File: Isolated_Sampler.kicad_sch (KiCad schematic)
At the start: 22 parts, among them U11 AMC1351, U13 TLV6002

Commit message: schematic: Assign all footprints
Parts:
- C42, C43: footprint (none) -> Capacitor_SMD:C_0603_1608Metric
- R74: footprint (none) -> Resistor_SMD:R_0603_1608Metric
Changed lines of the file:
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@@
 			)
 		)
-		(property "Footprint" ""
+		(property "Footprint" "Capacitor_SMD:C_0603_1608Metric"
 			(at 194.31 80.01 0)
 			(effects
@@
 			)
 		)
-		(property "Footprint" ""
+		(property "Footprint" "Resistor_SMD:R_0603_1608Metric"
 			(at 185.42 114.3 0)
 			(effects
@@
 			)
 		)
-		(property "Footprint" ""
+		(property "Footprint" "Capacitor_SMD:C_0603_1608Metric"
 			(at 180.34 114.3 0)
 			(effects

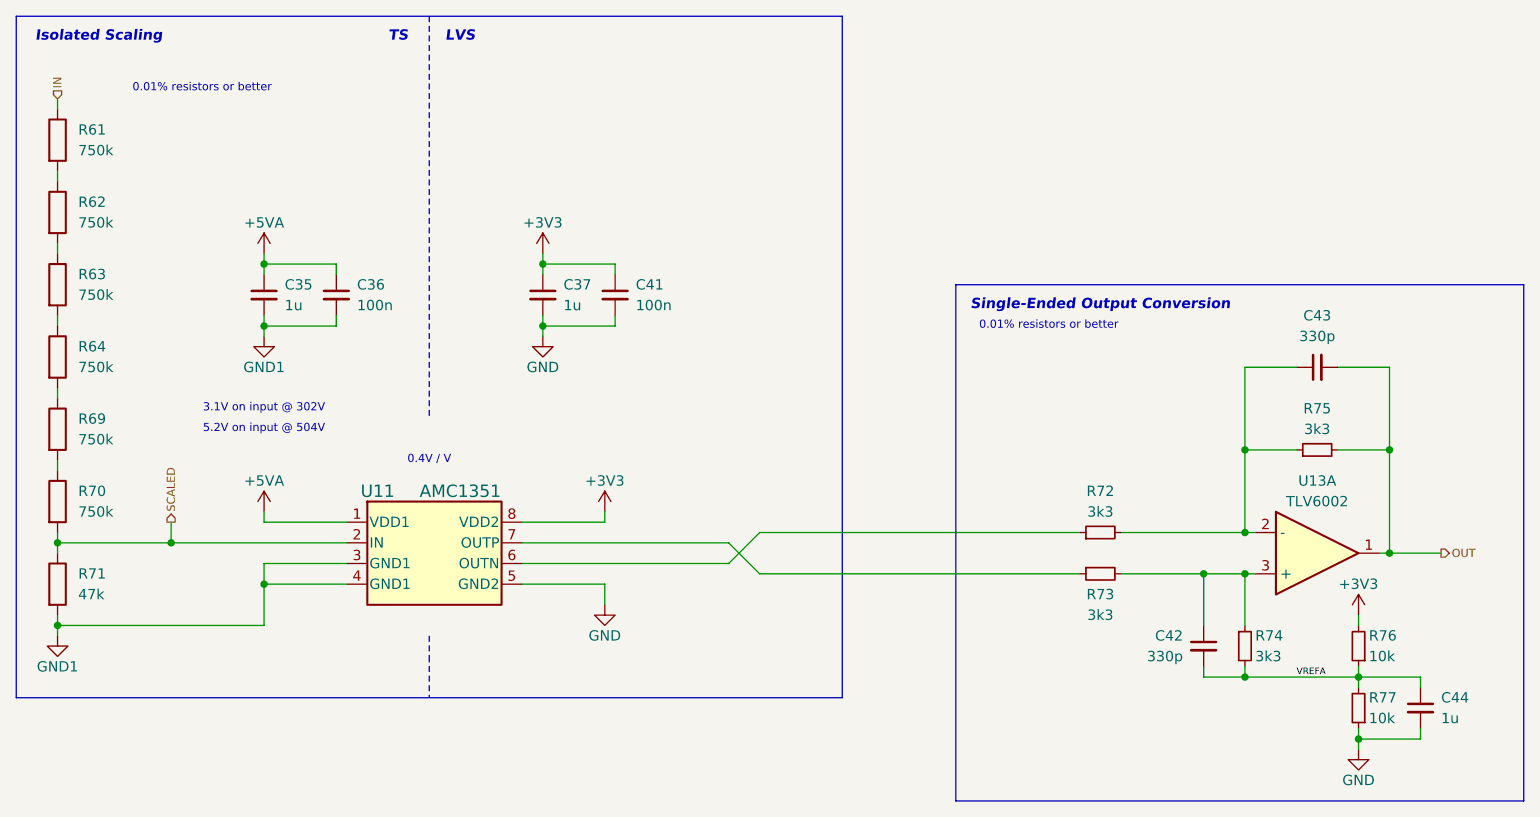
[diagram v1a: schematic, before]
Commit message: schematic: Reassign reference designators
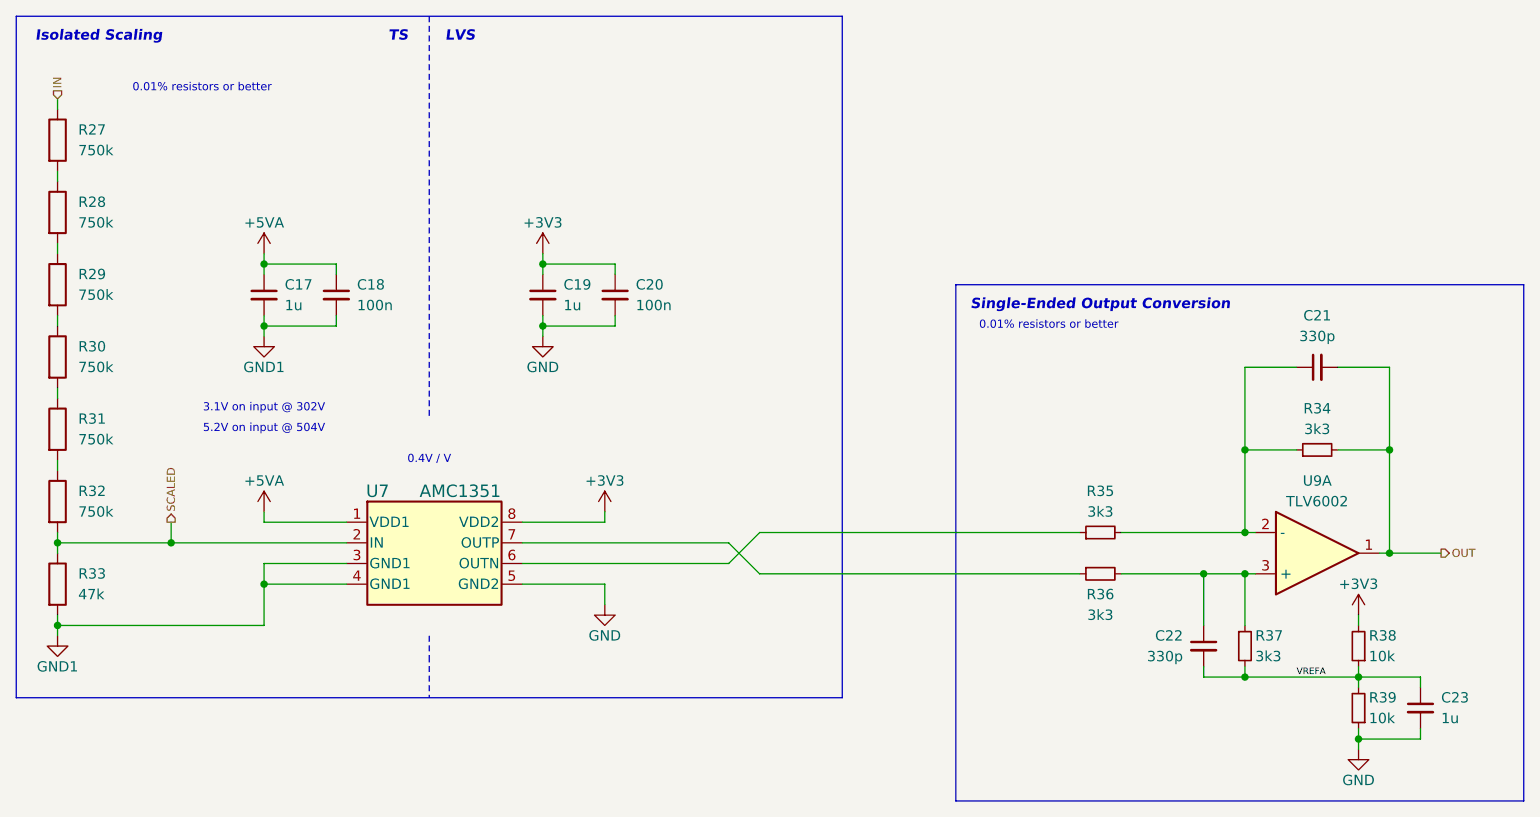
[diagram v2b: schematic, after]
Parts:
- renumbered C35 to C17, C36 to C18, C37 to C19, C41 to C20, C43 to C21, C42 to C22, C44 to C23, R61 to R27, R62 to R28, R63 to R29, R64 to R30, R69 to R31, R70 to R32, R71 to R33, R75 to R34, R72 to R35, R73 to R36, R74 to R37, R76 to R38, R77 to R39, U11 to U7, U13 to U9

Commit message: schematic: Fill out most of the BOM
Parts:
- C18, C20: Dist # C5199872 -> C1591; Mfr # CL10B105KB8NQNC -> CL10B104KB8NNNC
- C23: Dist (none) -> LCSC; Dist # (none) -> C5199872; Mfr (none) -> Samsung; Mfr # (none) -> CL10B105KB8NQNC
- R38, R39: Dist (none) -> LCSC; Dist # (none) -> C25804; Mfr (none) -> Uni-Royal; Mfr # (none) -> 0603WAF1002T5E
- U7: Dist (none) -> Mouser; Dist # (none) -> 595-AMC1351QDWVRQ1; Mfr (none) -> Texas Instruments; Mfr # (none) -> AMC1351QDWVRQ1
- U9: Dist (none) -> Mouser; Dist # (none) -> 595-TLV6002QDRQ1; Mfr (none) -> Texas Instruments; Mfr # (none) -> TLV6002QDRQ1
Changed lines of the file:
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@@
 			)
 		)
-		(property "Dist #" "C5199872"
+		(property "Dist #" "C1591"
 			(at 107.95 71.12 0)
 			(effects
@@
 			)
 		)
-		(property "Mfr #" "CL10B105KB8NQNC"
+		(property "Mfr #" "CL10B104KB8NNNC"
 			(at 107.95 71.12 0)
 			(effects
@@
 			)
 		)
-		(property "Dist #" "C5199872"
+		(property "Dist #" "C1591"
 			(at 73.66 71.12 0)
 			(effects
@@
 			)
 		)
-		(property "Mfr #" "CL10B105KB8NQNC"
+		(property "Mfr #" "CL10B104KB8NNNC"
 			(at 73.66 71.12 0)
 			(effects
@@
 			)
 		)
+		(property "Dist" "Mouser"
+			(at 194.31 102.87 0)
+			(effects
+				(font
+					(size 1.27 1.27)
+				)
+				(hide yes)
+			)
+		)
+		(property "Dist #" "595-TLV6002QDRQ1"
+			(at 194.31 102.87 0)
+			(effects
+				(font
+					(size 1.27 1.27)
+				)
+				(hide yes)
+			)
+		)
+		(property "Mfr" "Texas Instruments"
+			(at 194.31 102.87 0)
+			(effects
+				(font
+					(size 1.27 1.27)
+				)
+				(hide yes)
+			)
+		)
+		(property "Mfr #" "TLV6002QDRQ1"
+			(at 194.31 102.87 0)
+			(effects
+				(font
+					(size 1.27 1.27)
+				)
+				(hide yes)
+			)
+		)
 		(pin "4"
 		)
@@
 			)
 		)
+		(property "Dist" "LCSC"
+			(at 207.01 121.92 0)
+			(effects
+				(font
+					(size 1.27 1.27)
+				)
+				(hide yes)
+			)
+		)
+		(property "Dist #" "C5199872"
+			(at 207.01 121.92 0)
+			(effects
+				(font
+					(size 1.27 1.27)
+				)
+				(hide yes)
+			)
+		)
+		(property "Mfr" "Samsung"
+			(at 207.01 121.92 0)
+			(effects
+				(font
+					(size 1.27 1.27)
+				)
+				(hide yes)
+			)
+		)
+		(property "Mfr #" "CL10B105KB8NQNC"
+			(at 207.01 121.92 0)
+			(effects
+				(font
+					(size 1.27 1.27)
+				)
+				(hide yes)
+			)
+		)
 		(pin "2"
 		)
@@
 			)
 		)
+		(property "Dist" "LCSC"
+			(at 199.39 114.3 0)
+			(effects
+				(font
+					(size 1.27 1.27)
+				)
+				(hide yes)
+			)
+		)
+		(property "Dist #" "C25804"
+			(at 199.39 114.3 0)
+			(effects
+				(font
+					(size 1.27 1.27)
+				)
+				(hide yes)
+			)
+		)
+		(property "Mfr" "Uni-Royal"
+			(at 199.39 114.3 0)
+			(effects
+				(font
+					(size 1.27 1.27)
+				)
+				(hide yes)
+			)
+		)
+		(property "Mfr #" "0603WAF1002T5E"
+			(at 199.39 114.3 0)
+			(effects
+				(font
+					(size 1.27 1.27)
+				)
+				(hide yes)
+			)
+		)
 		(pin "1"
 		)
@@
 		(property "Description" "Precision, 5-V Input, Reinforced Isolated Amplifier"
 			(at 77.216 77.978 0)
+			(effects
+				(font
+					(size 1.27 1.27)
+				)
+				(hide yes)
+			)
+		)
+		(property "Dist" "Mouser"
+			(at 77.47 96.52 0)
+			(effects
+				(font
+					(size 1.27 1.27)
+				)
+				(hide yes)
+			)
+		)
+		(property "Dist #" "595-AMC1351QDWVRQ1"
+			(at 77.47 96.52 0)
+			(effects
+				(font
+					(size 1.27 1.27)
+				)
+				(hide yes)
+			)
+		)
+		(property "Mfr" "Texas Instruments"
+			(at 77.47 96.52 0)
+			(effects
+				(font
+					(size 1.27 1.27)
+				)
+				(hide yes)
+			)
+		)
+		(property "Mfr #" "AMC1351QDWVRQ1"
+			(at 77.47 96.52 0)
 			(effects
 				(font
@@
 			(at 199.39 121.92 0)
 			(effects
+				(font
+					(size 1.27 1.27)
+				)
+				(hide yes)
+			)
+		)
+		(property "Dist" "LCSC"
+			(at 199.39 121.92 0)
+			(effects
+				(font
+					(size 1.27 1.27)
+				)
+				(hide yes)
+			)
+		)
+		(property "Dist #" "C25804"
+			(at 199.39 121.92 0)
+			(effects
+				(font
+					(size 1.27 1.27)
+				)
+				(hide yes)
+			)
+		)
+		(property "Mfr" "Uni-Royal"
+			(at 199.39 121.92 0)
+			(effects
+				(font
+					(size 1.27 1.27)
+				)
+				(hide yes)
+			)
+		)
+		(property "Mfr #" "0603WAF1002T5E"
+			(at 199.39 121.92 0)
+			(effects

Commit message: pcb: Setup net classes and import components
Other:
- company: (none) -> York Formula Student
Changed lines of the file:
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@@
 	(paper "A4")
 	(title_block
+		(date "2025-12-13")
 		(rev "${REVISION}")
+		(company "York Formula Student")
+		(comment 1 "Designed by Josh B, Logan C, and Owen S")
 	)
 	(rectangle

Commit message: Revision A
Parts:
- R27, R28, R29, R30, R31, R32, R33: footprint Resistor_SMD:R_0805_2012Metric -> Resistor_SMD:R_1206_3216Metric
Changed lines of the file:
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@@
 			)
 		)
-		(property "Footprint" "Resistor_SMD:R_0805_2012Metric"
+		(property "Footprint" "Resistor_SMD:R_1206_3216Metric"
 			(at 37.592 78.74 90)
 			(effects
@@
 			)
 		)
-		(property "Footprint" "Resistor_SMD:R_0805_2012Metric"
+		(property "Footprint" "Resistor_SMD:R_1206_3216Metric"
 			(at 37.592 60.96 90)
 			(effects
@@
 			)
 		)
-		(property "Footprint" "Resistor_SMD:R_0805_2012Metric"
+		(property "Footprint" "Resistor_SMD:R_1206_3216Metric"
 			(at 37.592 87.63 90)
 			(effects
@@
 			)
 		)
-		(property "Footprint" "Resistor_SMD:R_0805_2012Metric"
+		(property "Footprint" "Resistor_SMD:R_1206_3216Metric"
 			(at 37.592 96.52 90)
 			(effects
@@
 			)
 		)
-		(property "Footprint" "Resistor_SMD:R_0805_2012Metric"
+		(property "Footprint" "Resistor_SMD:R_1206_3216Metric"
 			(at 37.592 106.68 90)
 			(effects
@@
 			)
 		)
-		(property "Footprint" "Resistor_SMD:R_0805_2012Metric"
+		(property "Footprint" "Resistor_SMD:R_1206_3216Metric"
 			(at 37.592 69.85 90)
 			(effects
@@
 			)
 		)
-		(property "Footprint" "Resistor_SMD:R_0805_2012Metric"
+		(property "Footprint" "Resistor_SMD:R_1206_3216Metric"
 			(at 37.592 52.07 90)
 			(effects

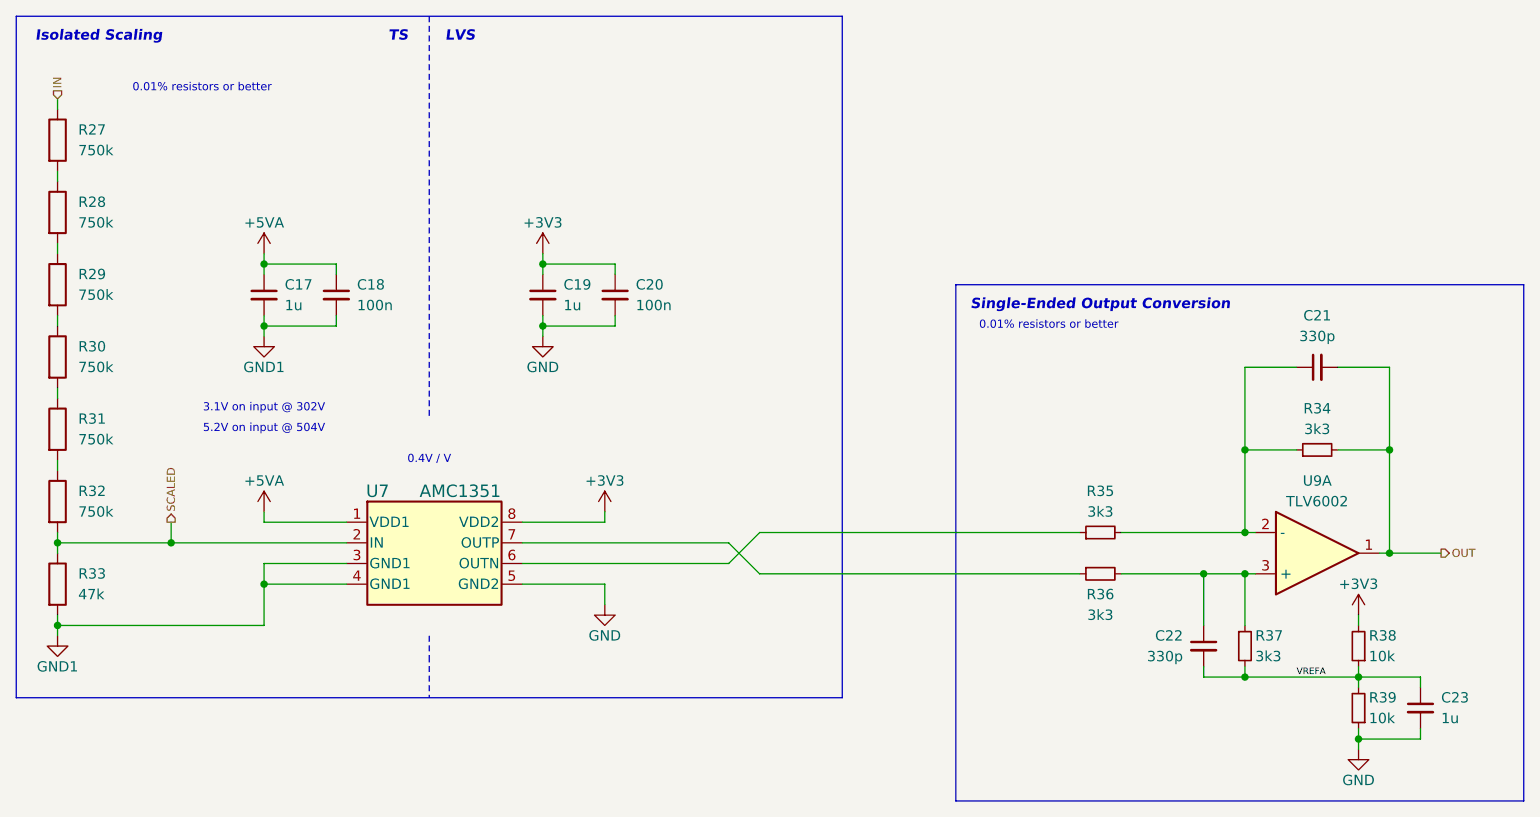
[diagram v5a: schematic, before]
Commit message: *: Add test points around sampling
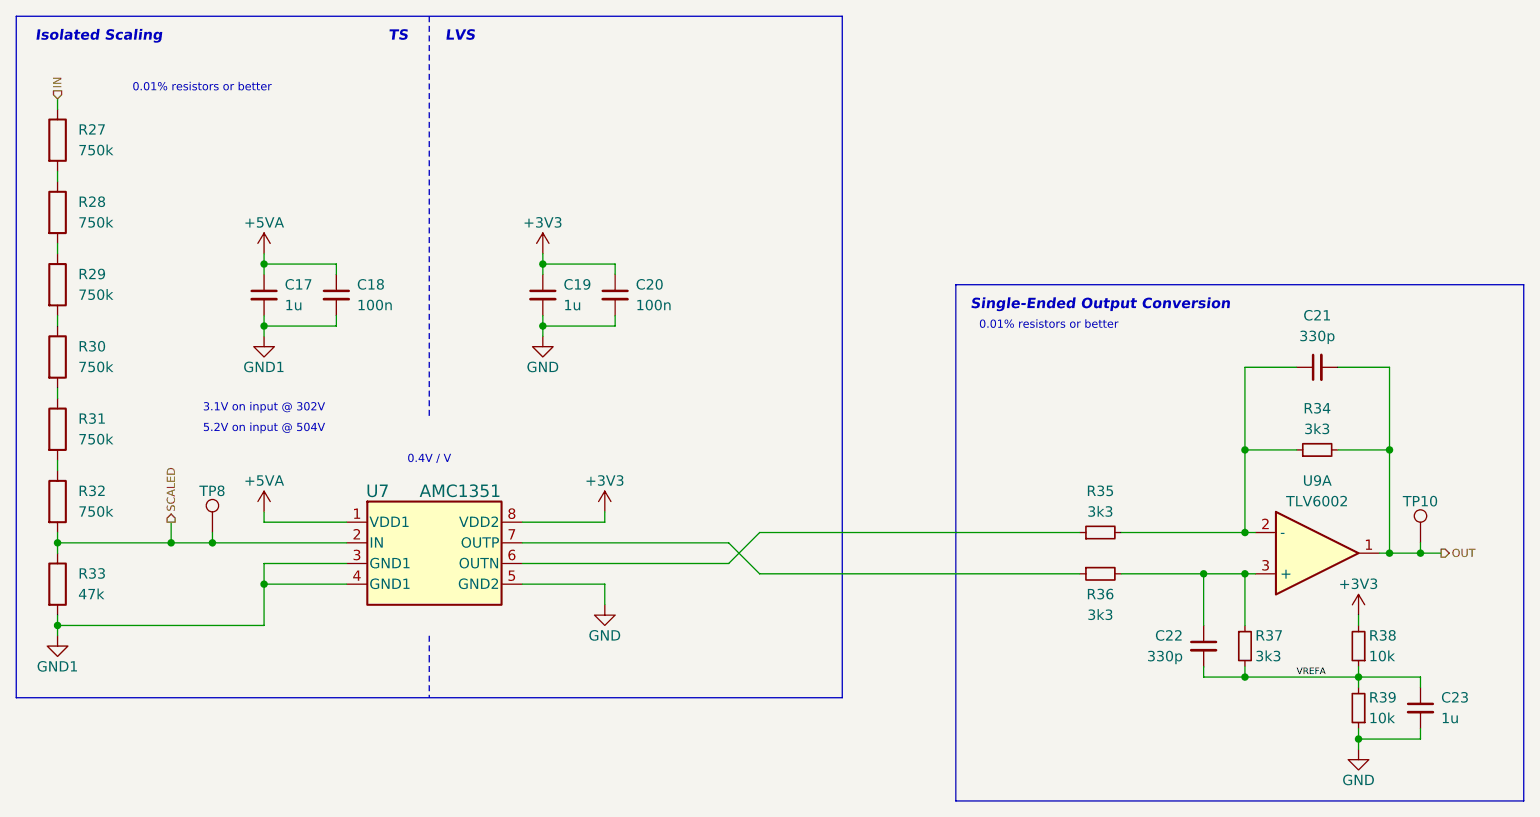
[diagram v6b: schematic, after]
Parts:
- added TP10, TP8: TestPoint, TestPoint:TestPoint_Keystone_5000-5004_Miniature, symbol Connector:TestPoint
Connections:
- net OUT: now also TP10.1
- net SCALED: now also TP8.1
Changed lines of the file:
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@@
+	)
+	(junction
+		(at 58.42 101.6)
+		(diameter 0)
+		(color 0 0 0 0)
 	)
 	(junction
@@
 	)
 	(junction
+		(at 207.01 102.87)
+		(diameter 0)
+		(color 0 0 0 0)
+	)
+	(junction
 		(at 180.34 105.41)
 		(diameter 0)
@@
 	(wire
 		(pts
+			(xy 58.42 100.33) (xy 58.42 101.6)
+		)
+		(stroke
+			(width 0)
+			(type default)
+		)
+	)
+	(wire
+		(pts
 			(xy 191.77 80.01) (xy 185.42 80.01)
 		)
@@
 	(wire
 		(pts
-			(xy 53.34 101.6) (xy 74.93 101.6)
+			(xy 53.34 101.6) (xy 58.42 101.6)
 		)
 		(stroke
@@
 	(wire
 		(pts
+			(xy 58.42 101.6) (xy 74.93 101.6)
+		)
+		(stroke
+			(width 0)
+			(type default)
+		)
+	)
+	(wire
+		(pts
 			(xy 203.2 80.01) (xy 203.2 90.17)
 		)
@@
 	(wire
 		(pts
-			(xy 203.2 102.87) (xy 209.55 102.87)
+			(xy 207.01 102.87) (xy 209.55 102.87)
+		)
+		(stroke
+			(width 0)
+			(type default)
+		)
+	)
+	(wire
+		(pts
+			(xy 203.2 102.87) (xy 207.01 102.87)
 		)
 		(stroke
@@
 		(pts
 			(xy 64.77 66.04) (xy 64.77 67.31)
+		)
+		(stroke
+			(width 0)
+			(type default)
+		)
+	)
+	(wire
+		(pts
+			(xy 207.01 101.6) (xy 207.01 102.87)
 		)
 		(stroke
@@
 	)
 	(symbol
+		(lib_id "Connector:TestPoint")
+		(at 207.01 101.6 0)
+		(unit 1)
+		(exclude_from_sim no)
+		(in_bom yes)
+		(on_board yes)
+		(dnp no)
+		(property "Reference" "TP10"
+			(at 207.01 96.52 0)
+			(effects
+				(font
+					(size 1.27 1.27)
+				)
+			)
+		)
+		(property "Value" "TestPoint"
+			(at 209.55 99.5679 0)
+			(effects
+				(font
+					(size 1.27 1.27)
+				)
+				(justify left)
+				(hide yes)
+			)
+		)
+		(property "Footprint" "TestPoint:TestPoint_Keystone_5000-5004_Miniature"
+			(at 212.09 101.6 0)
+			(effects
+				(font
+					(size 1.27 1.27)
+				)
+				(hide yes)
+			)
+		)
+		(property "Datasheet" "~"
+			(at 212.09 101.6 0)
+			(effects
+				(font
+					(size 1.27 1.27)
+				)
+				(hide yes)
+			)
+		)
+		(property "Description" "test point"
+			(at 207.01 101.6 0)
+			(effects
+				(font
+					(size 1.27 1.27)
+				)
+				(hide yes)
+			)
+		)
+		(pin "1"
+		)
+		(instances
+			(project "Precharge_PCB"
+				(path "/c467677d-b98c-4488-bd11-965ef67263b2/5111e28e-8231-41c0-b506-a567affaf28a/40675a50-a5c6-4759-acd6-914b3ce60c39"
+					(reference "TP10")
+					(unit 1)
+				)
+				(path "/c467677d-b98c-4488-bd11-965ef67263b2/5111e28e-8231-41c0-b506-a567affaf28a/481c6b85-c613-4759-b3cf-851f0c736d9a"
+					(reference "TP11")
+					(unit 1)
+				)
+			)
+		)
+	)
+	(symbol
 		(lib_id "Device:R_Small")
 		(at 167.64 100.33 90)
@@
 					(unit 1)
 				)
+			)
+		)
+	)
+	(symbol
+		(lib_id "Connector:TestPoint")
+		(at 58.42 100.33 0)
+		(unit 1)
+		(exclude_from_sim no)
+		(in_bom yes)
+		(on_board yes)
+		(dnp no)
+		(property "Reference" "TP8"
+			(at 58.42 95.25 0)
+			(effects
+				(font
+					(size 1.27 1.27)
+				)
+			)
+		)
+		(property "Value" "TestPoint"
+			(at 60.96 98.2979 0)
+			(effects
+				(font
+					(size 1.27 1.27)
+				)
+				(justify left)
+				(hide yes)
+			)
+		)
+		(property "Footprint" "TestPoint:TestPoint_Keystone_5000-5004_Miniature"
+			(at 63.5 100.33 0)
+			(effects
+				(font
+					(size 1.27 1.27)
+				)
+				(hide yes)
+			)
+		)
+		(property "Datasheet" "~"
+			(at 63.5 100.33 0)
+			(effects
+				(font
+					(size 1.27 1.27)
+				)
+				(hide yes)
+			)
+		)
+		(property "Description" "test point"
+			(at 58.42 100.33 0)
+			(effects
+				(font
+					(size 1.27 1.27)
+				)
+				(hide yes)
+			)
+		)
+		(pin "1"
+		)
+		(instances
+			(project "Precharge_PCB"
+				(path "/c467677d-b98c-4488-bd11-965ef67263b2/5111e28e-8231-41c0-b506-a567affaf28a/40675a50-a5c6-4759-acd6-914b3ce60c39"
+					(reference "TP8")
+					(unit 1)
+				)
+				(path "/c467677d-b98c-4488-bd11-965ef67263b2/5111e28e-8231-41c0-b506-a567affaf28a/481c6b85-c613-4759-b3cf-851f0c736d9a"
+					(reference "TP9")
+					(unit 1)
+				)
